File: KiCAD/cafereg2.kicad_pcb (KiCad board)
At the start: 4 copper layers, 56.7 x 31.9 mm, 76 parts, among them IC1 SiC431CED-T1-GE3, IC2 SiC431CED-T1-GE3, IC3 TPS63810YFFR, IC4 MUN3CAD03-SE

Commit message: Fix problems with the PCB
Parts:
- moved L3 3.14 mm to (147.1, 68.3), turned to 0 degrees
- moved C39 2.76 mm to (143.0, 71.7)
- moved 3v3 1.80 mm to (151.4, 72.6)
- moved C40 1.23 mm to (150.7, 69.1)
- moved IC3 0.96 mm to (147.1, 71.7), turned to 90 degrees
- moved C41 0.89 mm to (152.2, 69.1)
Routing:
- net GND: track 5.27 -> 3.30 mm, vias 114 -> 227
- net /TPS63810 3.3V 2.5A/3.3V: track 1.72 -> 0.00 mm
- net /SiC438 1.15V 8A/1.15V: track 20.0 -> 20.6 mm, vias 35 -> 66
- net VIN: track 18.5 -> 18.0 mm, vias 44 -> 46
- net Net-(IC3-LX2_1): track 2.35 -> 1.90 mm, vias 0 -> 4
- net Net-(IC3-LX1_1): track 2.32 -> 2.21 mm, vias 0 -> 4
- net /SiC431 1V 20A/1V: vias 38 -> 87
- added copper zone on B.Cu, net Net-(IC3-LX1_1)
- added copper zone on F.Cu, net Net-(IC3-LX1_1)
- added copper zone on B.Cu, net Net-(IC3-LX2_1)
- added copper zone on F.Cu, net Net-(IC3-LX2_1)

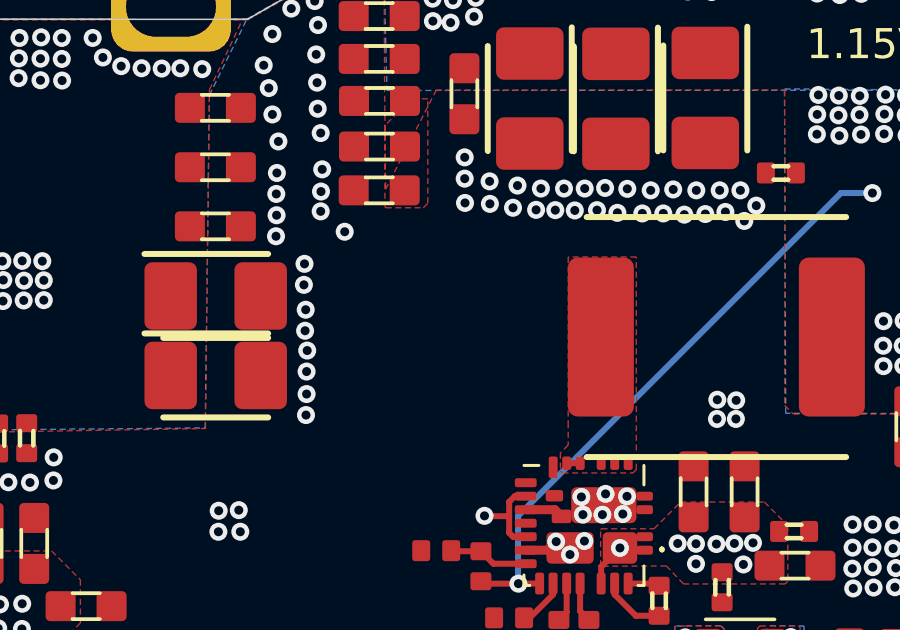
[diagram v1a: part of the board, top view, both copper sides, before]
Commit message: Add jig and my name to the silkscreen
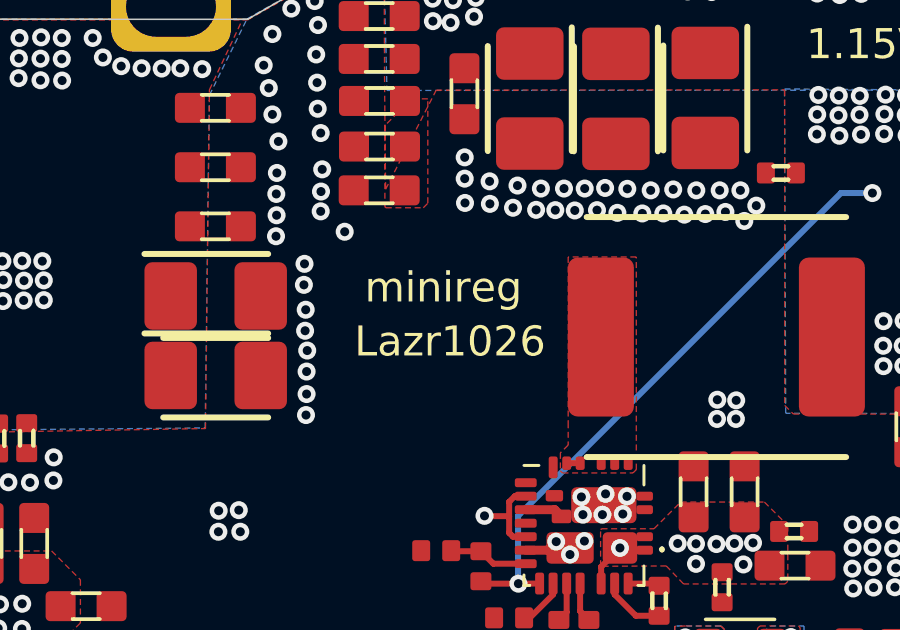
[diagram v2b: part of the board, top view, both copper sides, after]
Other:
- board text added: "Lazr1026"
- board text added: "minireg"
